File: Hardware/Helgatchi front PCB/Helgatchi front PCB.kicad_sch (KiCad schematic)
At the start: 31 parts, among them J1 BATTERY, J2 SCREEN, M1 MOTOR, Q1 NMOS, SW1 LEFT BUTTON, SW2 CENTER BUTTON, SW3 RIGHT BUTTON, U1 XIAO ESP32-S3

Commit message: Front PCB r2.7 order
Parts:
- D1, D8, D9: LCSC Part # C25803 -> C7420320
- H1, H2: now in the parts list
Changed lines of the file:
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@@
 			)
 		)
-		(property "LCSC Part #" "C25803"
+		(property "LCSC Part #" "C7420320"
 			(at 68.58 55.88 90)
 			(effects
@@
 		(unit 1)
 		(exclude_from_sim no)
-		(in_bom no)
+		(in_bom yes)
 		(on_board yes)
 		(dnp no)
@@
 		(unit 1)
 		(exclude_from_sim no)
-		(in_bom no)
+		(in_bom yes)
 		(on_board yes)
 		(dnp no)
@@
 			)
 		)
-		(property "LCSC Part #" "C25803"
+		(property "LCSC Part #" "C7420320"
 			(at 68.58 71.12 90)
 			(effects
@@
 			)
 		)
-		(property "LCSC Part #" "C25803"
+		(property "LCSC Part #" "C7420320"
 			(at 68.58 128.27 0)
 			(effects

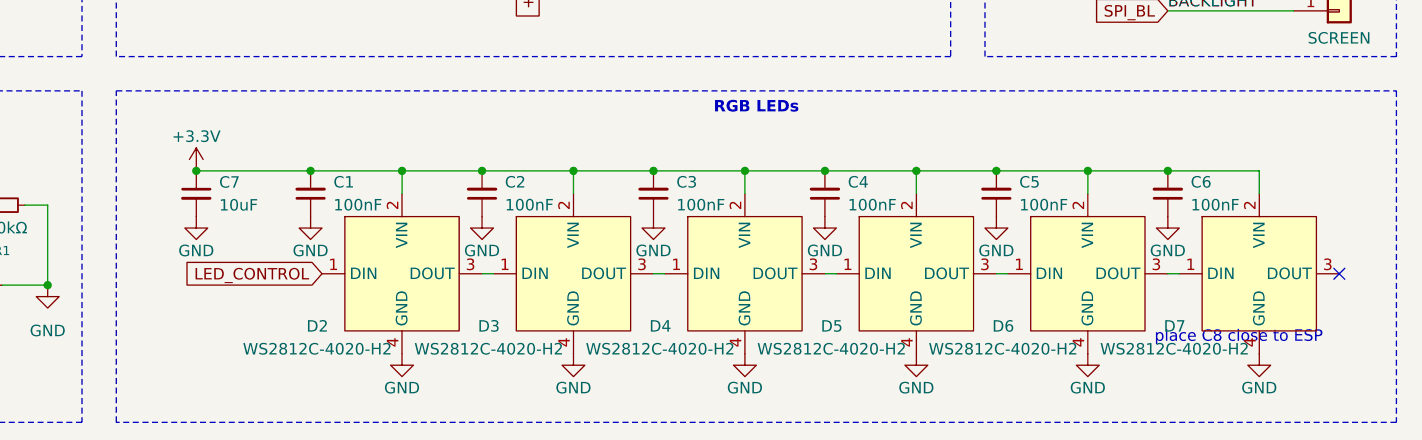
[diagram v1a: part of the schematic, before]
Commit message: Start of R2.8
- Moving to SK6805s for LEDs
- imported footprint, symbol, and 3D model for SK6805-SIDE
- updated footprints and symbols for LEDs
- repositioned LEDs and capacitors
- Swapped LED chain direction to accommodate easier routing with new pinout
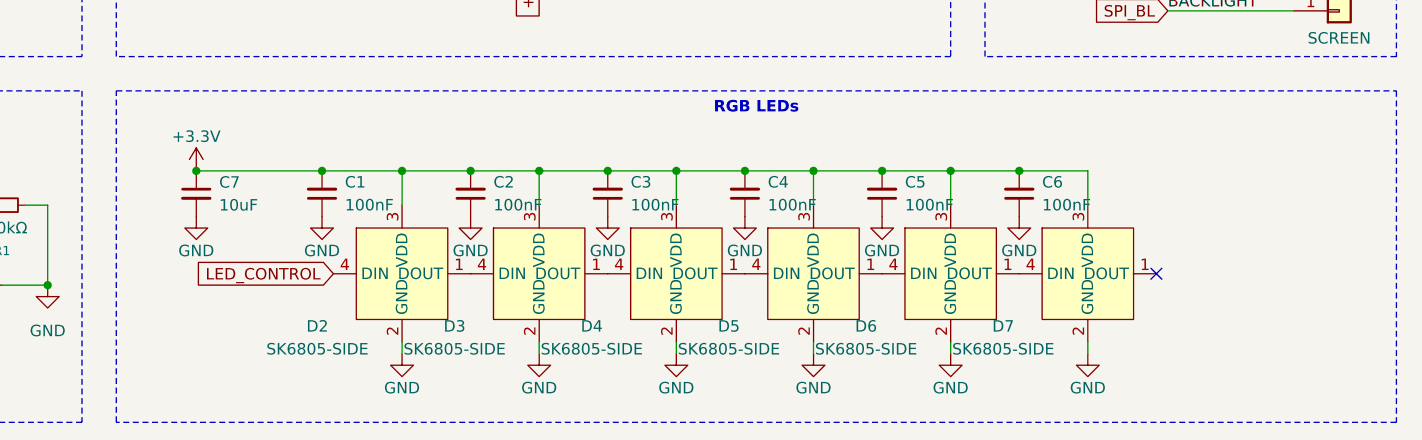
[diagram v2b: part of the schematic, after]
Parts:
- D2, D3, D4, D5, D6, D7: value WS2812C-4020-H2 -> SK6805-SIDE; footprint WS2812:WS2812C-4020-H2 -> SK68XX-SIDE:LED-SMD_4P-L3.5-W1.6_SK6805SIDE-G-001; symbol WS2812:WS2812B-4020 -> SK68XX-SIDE:SK6805SIDE-G-003; LCSC Part (none) -> C31452139; MPN (none) -> SK6805SIDE-G-003; Manufacturer (none) -> 欧思科光电
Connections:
- net +3.3V: now also D2.3 (VDD), D3.3 (VDD), D4.3 (VDD), D5.3 (VDD), D6.3 (VDD), D7.3 (VDD); no longer D2.2 (VIN), D3.2 (VIN), D4.2 (VIN), D5.2 (VIN), D6.2 (VIN), D7.2 (VIN)
- net GND: now also D2.2 (GND), D3.2 (GND), D4.2 (GND), D5.2 (GND), D6.2 (GND), D7.2 (GND); no longer D2.4 (GND), D3.4 (GND), D4.4 (GND), D5.4 (GND), D6.4 (GND), D7.4 (GND)
- net LED_CONTROL: now also D2.4 (DIN); no longer D2.1 (DIN)
- net at D7.1 (DOUT): no longer D6.3 (DOUT)
- net at D4.1 (DOUT): now also D5.4 (DIN); no longer D3.3 (DOUT)
- net at D5.1 (DOUT): now also D6.4 (DIN); no longer D4.3 (DOUT)
- net at D6.1 (DOUT): now also D7.4 (DIN); no longer D5.3 (DOUT)
- net at D3.1 (DOUT): now also D4.4 (DIN); no longer D2.3 (DOUT)
- new net: D2.1 (DOUT), D3.4 (DIN)
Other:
- note removed: "place C8 close to ESP"
- moved on the sheet: C1, C2, C3, C4, C5, C6, D3, D4, D5, D6, D7

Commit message: Commit new UI files
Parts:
- added TP1: BATT, TestPoint:TestPoint_Pad_D1.0mm, symbol Connector:TestPoint
- R4: now not fitted; now left out of the parts list
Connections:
- net +BATT: now also TP1.1
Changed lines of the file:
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@@
 		)
 	)
+	(global_label "+BATT"
+		(shape input)
+		(at 31.75 168.91 0)
+		(fields_autoplaced yes)
+		(effects
+			(font
+				(size 1.27 1.27)
+			)
+			(justify left)
+		)
+		(property "Intersheetrefs" "${INTERSHEET_REFS}"
+			(at 40.6014 168.91 0)
+			(hide yes)
+			(show_name no)
+			(do_not_autoplace no)
+			(effects
+				(font
+					(size 1.27 1.27)
+				)
+				(justify left)
+			)
+		)
+	)
 	(global_label "BUTTONS_1"
 		(shape bidirectional)
@@
 		(in_pos_files yes)
 		(dnp no)
-		(fields_autoplaced yes)
 		(property "Reference" "D9"
-			(at 71.12 54.6099 90)
+			(at 70.612 54.61 90)
 			(show_name no)
 			(do_not_autoplace no)
@@
 		)
 		(property "Value" "D_Schottky"
-			(at 71.12 57.1499 90)
+			(at 70.612 57.15 90)
 			(show_name no)
 			(do_not_autoplace no)
@@
 		(dnp no)
 		(property "Reference" "D8"
-			(at 73.66 69.85 90)
+			(at 71.374 69.596 90)
 			(show_name no)
 			(do_not_autoplace no)
@@
 		)
 		(property "Value" "D_Schottky"
-			(at 73.66 72.39 90)
+			(at 75.184 71.882 90)
 			(show_name no)
 			(do_not_autoplace no)
@@
 	)
 	(symbol
+		(lib_id "Connector:TestPoint")
+		(at 31.75 168.91 90)
+		(unit 1)
+		(body_style 1)
+		(exclude_from_sim no)
+		(in_bom yes)
+		(on_board yes)
+		(in_pos_files yes)
+		(dnp no)
+		(fields_autoplaced yes)
+		(property "Reference" "TP1"
+			(at 28.448 163.83 90)
+			(show_name no)
+			(do_not_autoplace no)
+			(effects
+				(font
+					(size 1.27 1.27)
+				)
+			)
+		)
+		(property "Value" "BATT"
+			(at 28.448 166.37 90)
+			(show_name no)
+			(do_not_autoplace no)
+			(effects
+				(font
+					(size 1.27 1.27)
+				)
+			)
+		)
+		(property "Footprint" "TestPoint:TestPoint_Pad_D1.0mm"
+			(at 31.75 163.83 0)
+			(hide yes)
+			(show_name no)
+			(do_not_autoplace no)
+			(effects
+				(font
+					(size 1.27 1.27)
+				)
+			)
+		)
+		(property "Datasheet" ""
+			(at 31.75 163.83 0)
+			(hide yes)
+			(show_name no)
+			(do_not_autoplace no)
+			(effects
+				(font
+					(size 1.27 1.27)
+				)
+			)
+		)
+		(property "Description" "test point"
+			(at 31.75 168.91 0)
+			(hide yes)
+			(show_name no)
+			(do_not_autoplace no)
+			(effects
+				(font
+					(size 1.27 1.27)
+				)
+			)
+		)
+		(pin "1"
+		)
+		(instances
+			(project "Helgatchi front PCB"
+				(path "/b327183b-637b-47aa-8f80-c4d41dce62b6"
+					(reference "TP1")
+					(unit 1)
+				)
+			)
+		)
+	)
+	(symbol
 		(lib_id "power:GND")
 		(at 139.7 125.73 0)
@@
 		(body_style 1)
 		(exclude_from_sim no)
-		(in_bom yes)
+		(in_bom no)
 		(on_board yes)
 		(in_pos_files yes)
-		(dnp no)
+		(dnp yes)
 		(fields_autoplaced yes)
 		(property "Reference" "R4"

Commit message: final R2.9 revision, boards ordered
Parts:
- removed C7: 10uF, Capacitor_SMD:C_0603_1608Metric, symbol Device:C_Small
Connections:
- net +3.3V: no longer C1.2, C2.2, C3.2, C4.2, C5.2, C6.2, D1.1 (K), D2.3 (VDD), D3.3 (VDD), D4.3 (VDD), D5.3 (VDD), D6.3 (VDD), D7.3 (VDD), M1.1 (+)
- net +BATT: now also C1.2, C2.2, C3.2, C4.2, C5.2, C6.2, D1.1 (K), D2.3 (VDD), D3.3 (VDD), D4.3 (VDD), D5.3 (VDD), D6.3 (VDD), D7.3 (VDD), M1.1 (+)
